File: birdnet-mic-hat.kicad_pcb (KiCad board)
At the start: 4 copper layers, 17.8 x 22.7 mm, 28 parts, among them J1 PJ-327A0-SMT, J3 DF40HC(3.5)-30DS-0.4V(51), U1 TLV320ADC5140, U2 TPS7A2033PDBVR, U3 TLV3691IDCKR

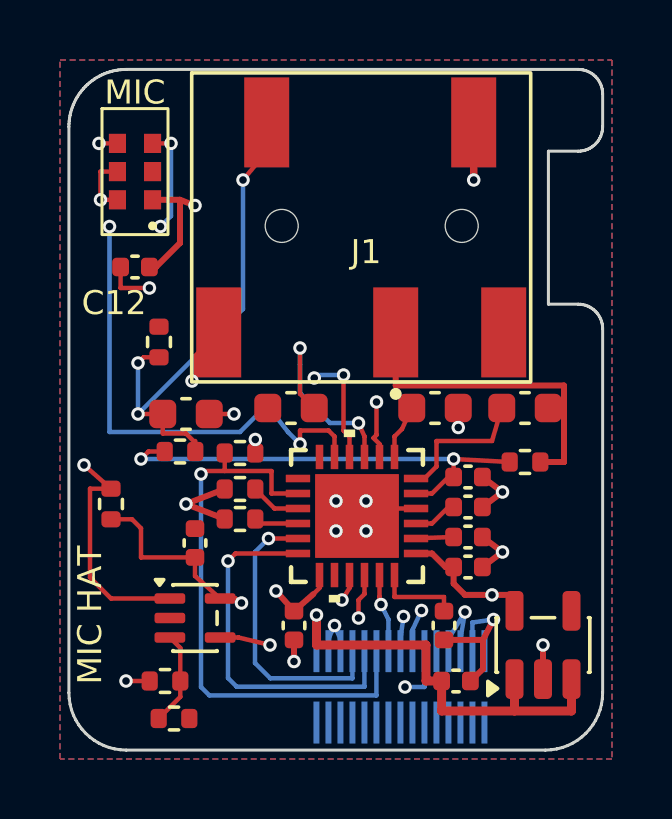
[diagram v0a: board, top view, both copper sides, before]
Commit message: Replace jack detector comparator with transistor and removable link
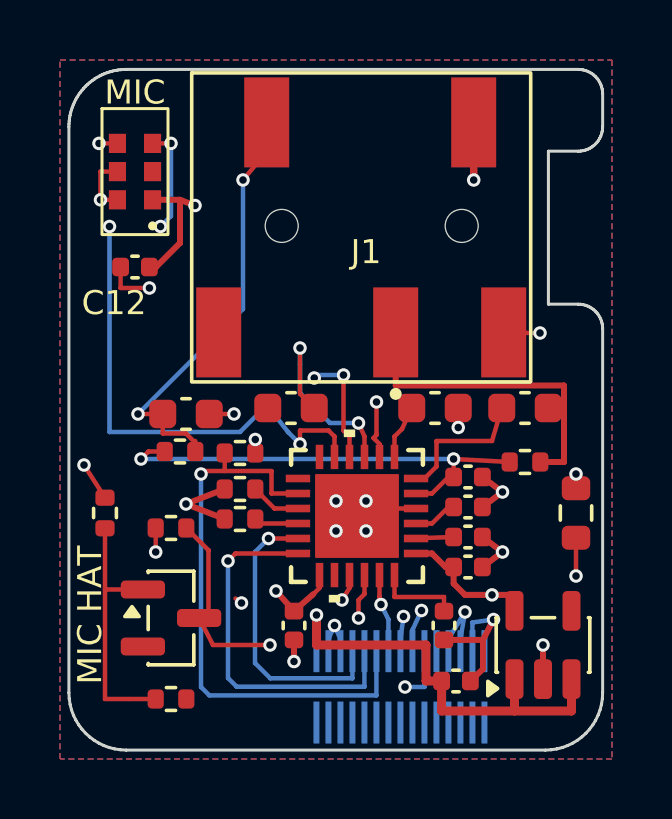
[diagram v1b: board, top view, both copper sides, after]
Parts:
- removed C13: 0.1uF, Capacitor_SMD:C_0402_1005Metric
- removed R9: 1M, Resistor_SMD:R_0402_1005Metric
- removed U3: TLV3691IDCKR, Package_TO_SOT_SMD:SOT-353_SC-70-5
- added Q1: MMBT3904, Package_TO_SOT_SMD:SOT-23, F.Cu at (103.5, 125.5)
- added R10: 0, Resistor_SMD:R_0603_1608Metric, F.Cu at (117.0, 122.0)
- R6: value 1M -> 47k
- R7: value 51k -> 100k
- moved R7 5.10 mm to (103.5, 122.5)
- moved R8 0.66 mm to (103.5, 128.2)
- moved R6 0.36 mm to (101.3, 122.0), turned to -90 degrees
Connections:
- J1 pad SW4: unconnected-(J1-X-PadSW4) -> Net-(J1-X)
- J1 pad SW6: /JACK_DET_RAW -> unconnected-(J1-RN-PadSW6)
- R6 pad 1: VCC_3V3 -> /JACK_BIAS_SENSE
- R6 pad 2: /JACK_DET_RAW -> Net-(Q1-B)
- R7 pad 2: /DET_THRESHOLD -> /MIC_PRESENT
- R8 pad 1: /DET_THRESHOLD -> Net-(Q1-B)
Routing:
- net /JACK_BIAS_SENSE: track 0.00 -> 31.4 mm, vias 0 -> 2
- net /JACK_DET_RAW: track 14.7 -> 0.00 mm, vias 2 -> 0
- net Net-(Q1-B): track 0.00 -> 8.64 mm
- net VCC_3V3: track 31.3 -> 23.5 mm
- net Net-(J1-X): track 0.00 -> 6.82 mm, vias 0 -> 2
- net /MIC_PRESENT: track 9.02 -> 13.9 mm
- net /DET_THRESHOLD: track 3.14 -> 0.00 mm
- net /JACK_RING: track 15.5 -> 13.1 mm, vias 3 -> 2

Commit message: Remove redundant jack detection link; retain 0402 base resistor
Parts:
- removed R10: 0, Resistor_SMD:R_0603_1608Metric
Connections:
- J1 pad SW4: Net-(J1-X) -> /JACK_BIAS_SENSE
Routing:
- net /JACK_BIAS_SENSE: track 31.4 -> 39.8 mm, vias 2 -> 4
- net Net-(J1-X): track 6.82 -> 0.00 mm, vias 2 -> 0
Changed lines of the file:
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@@
 		)
 	)
-	(footprint "Resistor_SMD:R_0603_1608Metric"
-		(layer "F.Cu")
-		(at 117 122 -90)
-		(descr "Resistor SMD 0603 (1608 Metric), square (rectangular) end terminal, IPC-7351 nominal, (Body size source: IPC-SM-782 page 72, https://www.pcb-3d.com/wordpress/wp-content/uploads/ipc-sm-782a_amendment_1_and_2.pdf)")
-		(tags "resistor")
-		(property "Reference" "R10"
-			(at 0 -1.43 -90)
-			(layer "F.SilkS")
-			(hide yes)
-			(effects
-				(font
-					(size 1 1)
-					(thickness 0.15)
-				)
-			)
-		)
-		(property "Value" "0"
-			(at 0 1.43 -90)
-			(layer "F.Fab")
-			(hide yes)
-			(effects
-				(font
-					(size 1 1)
-					(thickness 0.15)
-				)
-			)
-		)
-		(property "Datasheet" ""
-			(at 0 0 -90)
-			(layer "F.Fab")
-			(hide yes)
-			(effects
-				(font
-					(size 1.27 1.27)
-				)
-			)
-		)
-		(property "Description" "Remove to disable jack detection"
-			(at 0 0 -90)
-			(layer "F.Fab")
-			(hide yes)
-			(effects
-				(font
-					(size 1.27 1.27)
-				)
-			)
-		)
-		(property "KiLib_Generator" "SMD_2terminal_chip_molded"
-			(at 0 0 -90)
-			(layer "F.SilkS")
-			(hide yes)
-			(effects
-				(font
-					(size 1 1)
-					(thickness 0.15)
-				)
-			)
-		)
-		(property ki_fp_filters "R_*")
-		(sheetname "/")
-		(sheetfile "birdnet-mic-hat.kicad_sch")
-		(units
-			(unit
-				(name "A")
-				(pins "1" "2")
-			)
-		)
-		(attr smd)
-		(duplicate_pad_numbers_are_jumpers no)
-		(fp_line
-			(start -0.237258 0.5225)
-			(end 0.237258 0.5225)
-			(stroke
-				(width 0.12)
-				(type solid)
-			)
-			(layer "F.SilkS")
-		)
-		(fp_line
-			(start -0.237258 -0.5225)
-			(end 0.237258 -0.5225)
-			(stroke
-				(width 0.12)
-				(type solid)
-			)
-			(layer "F.SilkS")
-		)
-		(fp_rect
-			(start -1.48 -0.73)
-			(end 1.48 0.73)
-			(stroke
-				(width 0.05)
-				(type solid)
-			)
-			(fill no)
-			(layer "F.CrtYd")
-		)
-		(fp_rect
-			(start -0.8 -0.4125)
-			(end 0.8 0.4125)
-			(stroke
-				(width 0.1)
-				(type solid)
-			)
-			(fill no)
-			(layer "F.Fab")
-		)
-		(fp_text user "${REFERENCE}"
-			(at 0 0 -90)
-			(layer "F.Fab")
-			(effects
-				(font
-					(size 0.4 0.4)
-					(thickness 0.06)
-				)
-			)
-		)
-		(pad "1" smd roundrect
-			(at -0.825 0 270)
-			(size 0.8 0.95)
-			(layers "F.Cu" "F.Mask" "F.Paste")
-			(roundrect_rratio 0.25)
-			(net "Net-(J1-X)")
-			(pintype "passive")
-		)
-		(pad "2" smd roundrect
-			(at 0.825 0 270)
-			(size 0.8 0.95)
-			(layers "F.Cu" "F.Mask" "F.Paste")
-			(roundrect_rratio 0.25)
-			(net "/JACK_BIAS_SENSE")
-			(pintype "passive")
-		)
-		(embedded_fonts no)
-		(model "${KICAD10_3DMODEL_DIR}/Resistor_SMD.3dshapes/R_0603_1608Metric.step"
-			(offset
-				(xyz 0 0 0)
-			)
-			(scale
-				(xyz 1 1 1)
-			)
-			(rotate
-				(xyz 0 0 0)
-			)
-		)
-	)
 	(footprint "Capacitor_SMD:C_0402_1005Metric"
 		(layer "F.Cu")
@@
 			(size 1.5 3)
 			(layers "F.Cu" "F.Mask" "F.Paste")
-			(net "Net-(J1-X)")
+			(net "/JACK_BIAS_SENSE")
 			(pinfunction "X_SW4")
 			(pintype "passive")
@@
 	)
 	(segment
-		(start 115.5 116)
-		(end 115.8 116)
-		(width 0.15)
-		(layer "F.Cu")
-		(net "Net-(J1-X)")
-	)
-	(segment
-		(start 117 120.7)
-		(end 117 121.175)
-		(width 0.15)
-		(layer "F.Cu")
-		(net "Net-(J1-X)")
-	)
-	(segment
-		(start 114.59 115.98)
-		(end 115.5 116)
-		(width 0.15)
-		(layer "F.Cu")
-		(net "Net-(J1-X)")
-	)
-	(via
-		(at 115.8 116)
-		(size 0.45)
-		(drill 0.25)
-		(layers "F.Cu" "B.Cu")
-		(net "Net-(J1-X)")
-	)
-	(via
-		(at 117 120.7)
-		(size 0.45)
-		(drill 0.25)
-		(layers "F.Cu" "B.Cu")
-		(net "Net-(J1-X)")
-	)
-	(segment
-		(start 116.2 116.7)
-		(end 116.2 119.9)
-		(width 0.15)
-		(layer "In2.Cu")
-		(net "Net-(J1-X)")
-	)
-	(segment
-		(start 116.2 119.9)
-		(end 117 120.7)
-		(width 0.15)
-		(layer "In2.Cu")
-		(net "Net-(J1-X)")
-	)
-	(segment
-		(start 115.8 116)
-		(end 116.2 116.7)
-		(width 0.15)
-		(layer "In2.Cu")
-		(net "Net-(J1-X)")
-	)
-	(segment
 		(start 101.3 124.55)
 		(end 101.3 127.4)
@@
 	)
 	(segment
+		(start 117 121.175)
+		(end 117 122.825)
+		(width 0.15)
+		(layer "F.Cu")
+		(net "/JACK_BIAS_SENSE")
+	)
+	(segment
 		(start 117 122.825)
 		(end 117 124.1)
@@
 	)
 	(segment
+		(start 115.5 116)
+		(end 115.8 116)
+		(width 0.15)
+		(layer "F.Cu")
+		(net "/JACK_BIAS_SENSE")
+	)
+	(segment
+		(start 117 120.7)
+		(end 117 121.175)
+		(width 0.15)
+		(layer "F.Cu")
+		(net "/JACK_BIAS_SENSE")
+	)
+	(segment
 		(start 100.6 120.4)
 		(end 101.3 121.49)
@@
 		(net "/JACK_BIAS_SENSE")
 	)
+	(segment
+		(start 114.59 115.98)
+		(end 115.5 116)
+		(width 0.15)
+		(layer "F.Cu")
+		(net "/JACK_BIAS_SENSE")
+	)
+	(via
+		(at 115.8 116)
+		(size 0.45)
+		(drill 0.25)
+		(layers "F.Cu" "B.Cu")
+		(net "/JACK_BIAS_SENSE")
+	)
 	(via
 		(at 100.6 120.4)
@@
 		(net "/JACK_BIAS_SENSE")
 	)
+	(via
+		(at 117 120.7)
+		(size 0.45)
+		(drill 0.25)
+		(layers "F.Cu" "B.Cu")
+		(net "/JACK_BIAS_SENSE")
+	)
 	(segment
 		(start 101 120.8)
@@
 	)
 	(segment
+		(start 116.2 116.7)
+		(end 116.2 119.9)
+		(width 0.15)
+		(layer "In2.Cu")
+		(net "/JACK_BIAS_SENSE")
+	)
+	(segment
 		(start 116 129)
 		(end 101.5 129)
@@
 	)
 	(segment
+		(start 116.2 119.9)
+		(end 117 120.7)
+		(width 0.15)
+		(layer "In2.Cu")
+		(net "/JACK_BIAS_SENSE")
+	)
+	(segment
 		(start 116.5 128.5)
 		(end 116 129)
 		(width 0.15)
 		(layer "In2.Cu")
+		(net "/JACK_BIAS_SENSE")
+	)
+	(segment
+		(start 115.8 116)
+		(end 116.2 116.7)
+		(width 0.15)
+		(layer "In2.Cu")
